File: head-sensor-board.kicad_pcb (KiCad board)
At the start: 2 copper layers, 40 x 25 mm, 40 parts, among them J1 ToF_L (PLACEHOLDER), J2 ToF_R (PLACEHOLDER), J3 LED_L_EXT (1:+ 2:-), J4 LED_R_EXT (1:+ 2:-), Q1 AO3400A, Q2 AO3400A, U1 XIAO_ESP32S3_Sense

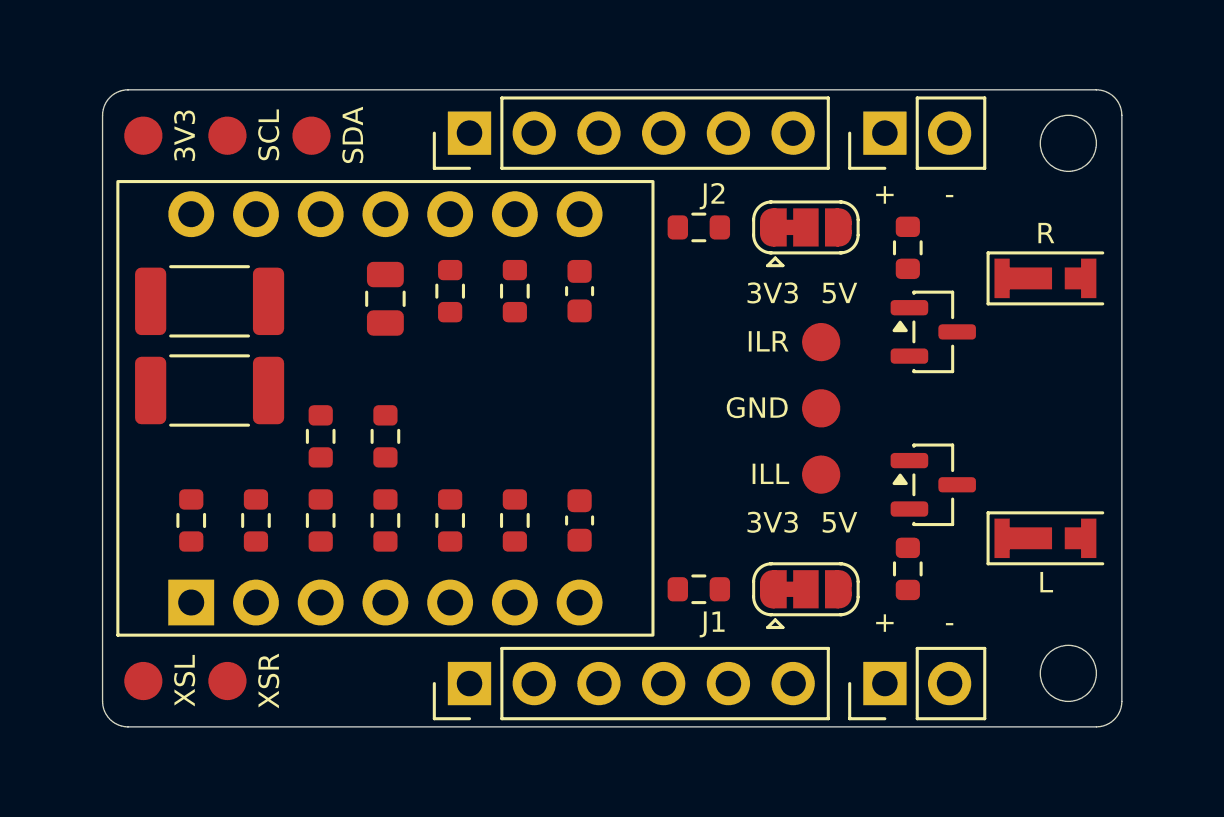
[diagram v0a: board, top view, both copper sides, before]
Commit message: Stage 4: 44x28 mm board, routing, DRC 0, 3D views (no gerbers/BOM/pos yet)
- Board outline 44x28 mm (corner R1, M2 x2 unchanged); placement revised for routability
  (J1/J2 rotated so SDA/SCL match XIAO order, SJ vertical, R3/R4 split by channel, TP5/TP6 moved).
- Silkscreen: L / R, USB-C arrow, J1/J2 six signal names (VIN GND SCL SDA XSHUT GPIO1).
- Auto-router (tools/route.py: numpy+scipy grid Dijkstra) + apply_routes.py + make_board.py.
  Power 0.5 mm, LED current paths 0.4 mm, signals 0.25 mm, GND pour both sides, 30 vias.
- DRC (schematic parity, --severity-all): 0 violations, 0 unconnected, 0 mismatches.
  Previously-ignored checks (missing courtyard, type/filter mismatch, via centering) set to error.
- J1/J2 use project footprint PinHeader_1x06_P2.54mm_NoSilk (standard silk outline removed).
- Simple 3D models (3dmodels/, illustration only), KiCad 3D renders, routed placement PNG.
- README: ToF module pinout fields + jumper-wire correspondence table (to fill when the module arrives).
- Sense expansion board vs placed parts checked from Seeed drawings (spec 6.5); camera/microSD protrusion unverified.

Co-Authored-By: Claude Sonnet 5.5 <noreply@anthropic.com>
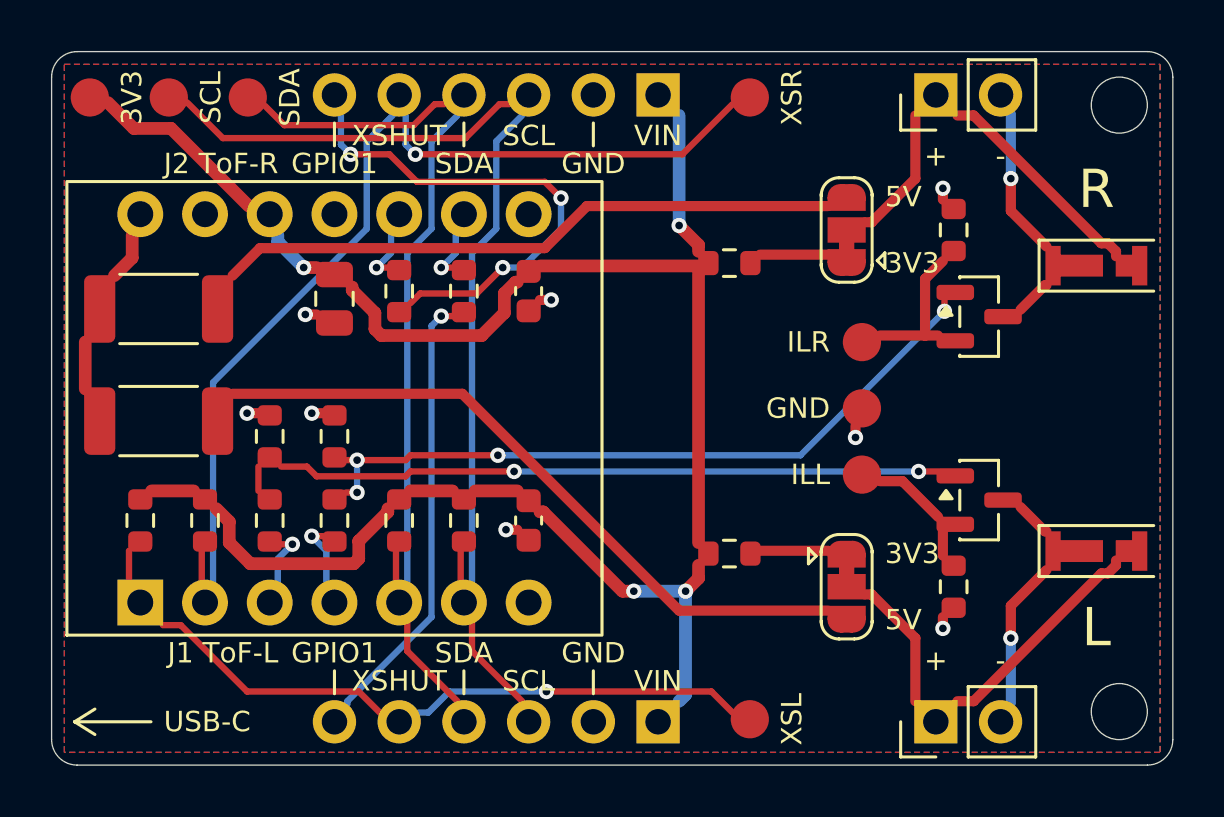
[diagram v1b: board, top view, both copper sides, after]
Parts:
- J1, J2: footprint Connector_PinHeader_2.54mm:PinHeader_1x06_P2.54mm_Vertical -> head-sensor-board:PinHeader_1x06_P2.54mm_NoSilk
- moved TP6 30.7 mm to (153.9, 92.8)
- moved TP5 23.8 mm to (153.9, 117.2)
- moved J1 7.55 mm to (150.3, 117.3), turned to -90 degrees
- moved J2 7.55 mm to (150.3, 92.7), turned to -90 degrees
- moved R3 5.11 mm to (130.7, 105.5)
- moved R4 3.77 mm to (130.7, 101.1)
- moved TP4 2.92 mm to (134.2, 92.8)
- moved TP3 2.75 mm to (131.1, 92.8)
- moved TP1 2.58 mm to (128.0, 92.8)
- moved H1 2.50 mm to (168.4, 93.1)
- moved H2 2.50 mm to (168.4, 116.9)
- moved J3 2.50 mm to (161.2, 117.3)
- moved J4 2.50 mm to (161.2, 92.7)
- moved D1 2.06 mm to (167.5, 110.6)
- moved D2 2.06 mm to (167.5, 99.4)
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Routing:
- net +3V3: track 0.00 -> 67.9 mm, vias 0 -> 4
- net /SCL: track 0.00 -> 37.9 mm
- net /XSHUT_R: track 0.00 -> 37.3 mm, vias 0 -> 1
- net /SDA: track 0.00 -> 31.8 mm
- net /GATE_R: track 0.00 -> 28.1 mm, vias 0 -> 4
- net /GATE_L: track 0.00 -> 27.0 mm, vias 0 -> 2
- net Net-(SJ1-B): track 0.00 -> 26.9 mm
- net Net-(SJ2-B): track 0.00 -> 24.5 mm
- net /XSHUT_L: track 0.00 -> 24.1 mm, vias 0 -> 1
- net /TOF_R_INT: track 0.00 -> 19.0 mm, vias 0 -> 3
- net /TOF_L_INT: track 0.00 -> 17.2 mm, vias 0 -> 1
- net /LEDA_R: track 0.00 -> 13.8 mm
- net /LEDA_L: track 0.00 -> 13.8 mm
- net /LEDK_R: track 0.00 -> 7.20 mm, vias 0 -> 1
- net /LEDK_L: track 0.00 -> 7.20 mm, vias 0 -> 1
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- added copper zone on B.Cu, net GND
- added copper zone on F.Cu, net GND
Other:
- board size 40 x 25 mm -> 44 x 28 mm
- board text added: "GPIO1"
- board text added: "J1 ToF-L"
- board text added: "J2 ToF-R"
- board text added: "TBC"
- board text added: "TOF PINS"
- board text added: "USB-C"
- board text added: "VIN"
- board text added: "XSHUT"
- board text removed: "TBD"
- board text removed: "TOF ORDER"

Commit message: Stage 4 final: silkscreen cleanup, manufacturing data in gerbers/ (not ordered)
- J1/J2 signal-name silk moved outside the header body (2.54 mm square), leader lines stop before it;
  J1/J2 pitched 0.25 mm closer to the board edge to make room. SJ and TP names also moved so
  they keep >= 0.1 mm from pads and other silk (tools/check_board.py, 137 silk items, 0 problems).
- check_board.py also verifies J1/J2 pad nets vs the schematic netlist vs silk names.
- gerbers/: Gerber (8 layers + job), Excellon PTH/NPTH, pos (SMD, non-DNP), BOM, ZIP, README, SHA256SUMS.
  Origin = board bottom-left. tools/verify_gerbers.py re-reads the ZIP with gerbonara and matches
  outline, 60 drill hits and copper against the board (all OK).
- Project DRC (schematic parity, all severities): 0 violations / 0 unconnected / 0 mismatches. ERC 0.
- Vias now 28 (20 signal + 8 GND stubs); docs/README/spec updated. Not ordered.

Co-Authored-By: Claude Sonnet 5.5 <noreply@anthropic.com>
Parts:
- moved J1 0.25 mm to (150.3, 117.5)
- moved J2 0.25 mm to (150.3, 92.5)
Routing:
- net +3V3: track 67.9 -> 77.1 mm, vias 4 -> 2
- net /TOF_R_INT: track 19.0 -> 19.7 mm
